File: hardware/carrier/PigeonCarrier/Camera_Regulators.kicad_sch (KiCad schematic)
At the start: 19 parts, among them U4 TPS62933FDRLR

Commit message: carrier progress
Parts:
- removed C31, C32, C39, C40, C41, C42, C44, C45: 10uF, Capacitor_SMD:C_1210_3225Metric, symbol Device:C
- removed C33, C38, C43, C46: 100nF, PCM_JLCPCB:C_0402, symbol PCM_JLCPCB-Capacitors:0402,100nF,(2)
- removed L1: 6.8uH, JLCImport_Auto:CYA1040-6_8UH, symbol JLCImport_Auto:CYA1040-6_8UH
- removed R11, R22: 10kΩ, PCM_JLCPCB:R_0402, symbol PCM_JLCPCB-Resistors:0402,10kΩ
- removed R14: 51kΩ, PCM_JLCPCB:R_0402, symbol PCM_JLCPCB-Resistors:0402,51kΩ
- removed R21: 1.5kΩ, PCM_JLCPCB:R_0402, symbol PCM_JLCPCB-Resistors:0402,1.5kΩ
- removed R23: 0Ω, PCM_JLCPCB:R_0402, symbol PCM_JLCPCB-Resistors:0402,0Ω
- removed U4: TPS62933FDRLR, PigeonVision:SOT-583-8, symbol PigeonVision:TPS62933FDRLR
- added C34, C35: 1uF, PCM_JLCPCB:C_0603, symbol PCM_JLCPCB-Capacitors:0603,1uF
- added C36, C37: 10uF, Capacitor_SMD:C_1210_3225Metric, symbol Device:C
- added R15: 7.5kΩ, PCM_JLCPCB:R_0402, symbol PCM_JLCPCB-Resistors:0402,7.5kΩ
- added R16, R17: 10kΩ, PCM_JLCPCB:R_0402, symbol PCM_JLCPCB-Resistors:0402,10kΩ
- added R18: 22kΩ, PCM_JLCPCB:R_0402, symbol PCM_JLCPCB-Resistors:0402,22kΩ
- added R19: 47kΩ, PCM_JLCPCB:R_0402, symbol PCM_JLCPCB-Resistors:0402,47kΩ
- added R24: 51kΩ, PCM_JLCPCB:R_0402, symbol PCM_JLCPCB-Resistors:0402,51kΩ
- added U6, U7: TLV75801PDRVR, PigeonVision:TI_DRV0006A_WSON-6-1EP_2x2mm_P0.65mm, symbol PigeonVision:TLV75801PDRVR
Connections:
- net GND: now also C34.1, C35.1, C36.2, C37.2, R15.2, R16.1, R17.1, R18.2, U6.3 (GND), U6.7 (GND), U7.3 (GND), U7.7 (GND)
- new net: R15.1, R19.2, U6.2 (FB)
- new net: R18.1, R24.2, U7.2 (FB)
- new net +3V3: C34.2, U7.6 (IN)
- new net 1V8_CAM: C37.1, R24.1, U7.1 (OUT)
- new net 1V8_CAM_EN: R16.2, U7.4 (EN)
- new net 4V_CAM: C36.1, R19.1, U6.1 (OUT)
- new net 4V_CAM_EN: R17.2, U6.4 (EN)
- new net 5V_MAIN: C35.2, U6.6 (IN)
- no-connect marks 1 -> 2
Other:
- note added: "1.825V Output"
- note added: "3.997V Output"
- note added: "3V3 -> 1V8"
- note added: "5V_Main-> 4V"
- note removed: "5.00V Output"
- note removed: "Effective Cap: 56.5uF"
- note removed: "Extra Caps to reduce ripple"
- note removed: "F_sw = 500kHz"
- note removed: "VBAT -> 5V_RF"
- note removed: "t_ss= 14.5ms ~19mA"
- note removed: "~4mV ripple W ESR"

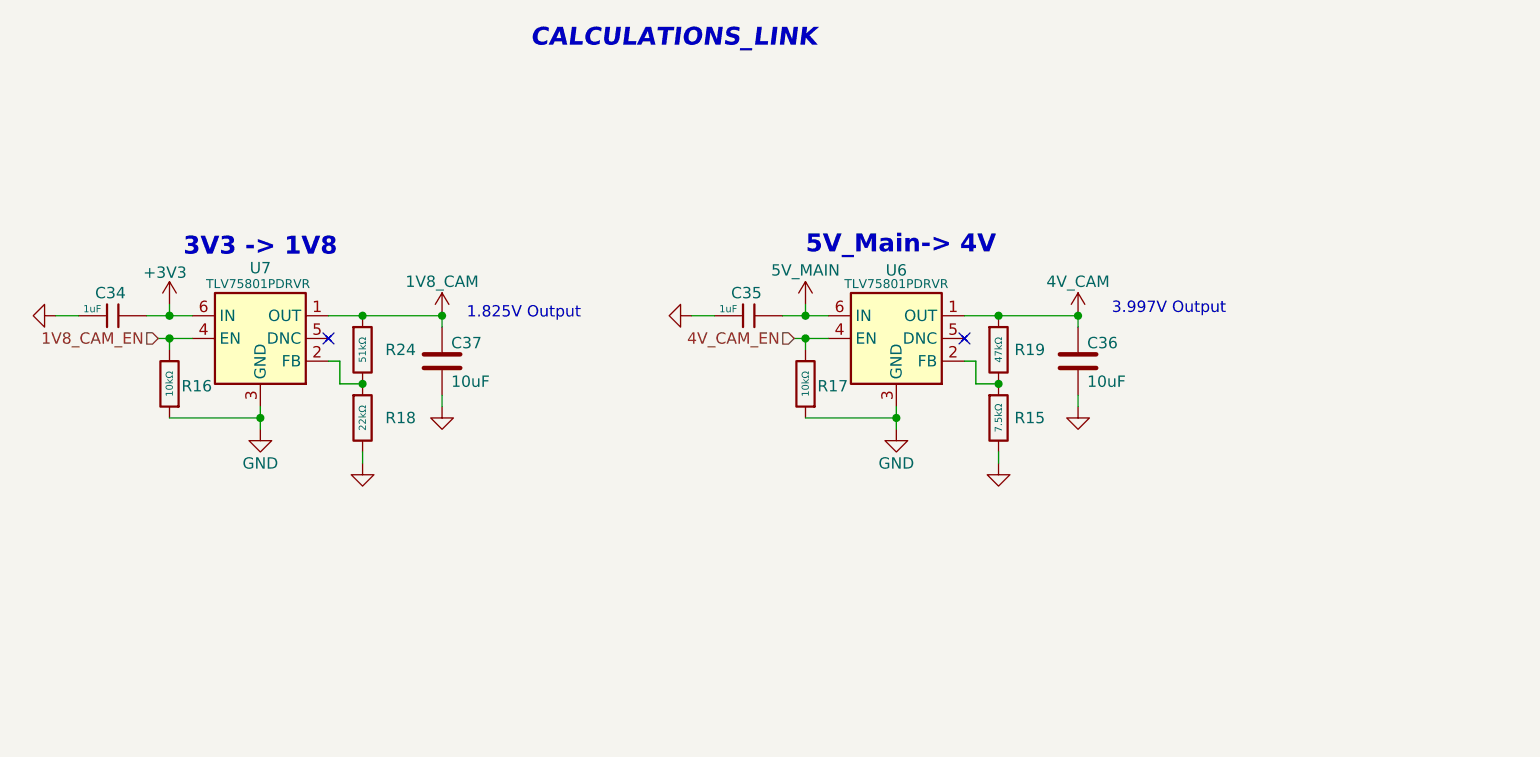
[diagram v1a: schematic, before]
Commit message: Update carrier schematics, parts library, and JLC rules
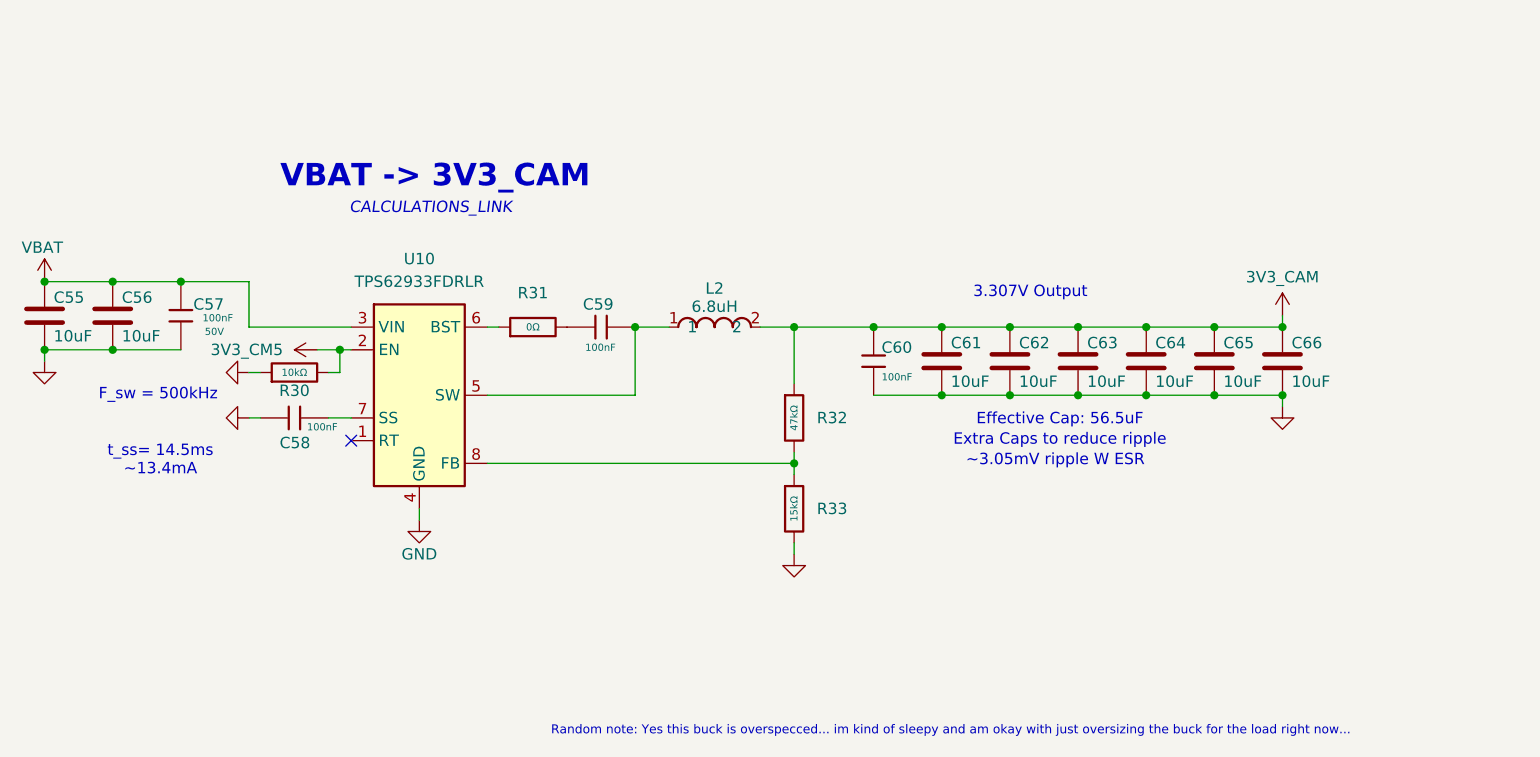
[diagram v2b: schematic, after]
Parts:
- removed C34, C35: 1uF, PCM_JLCPCB:C_0603, symbol PCM_JLCPCB-Capacitors:0603,1uF
- removed C36, C37: 10uF, Capacitor_SMD:C_1210_3225Metric, symbol Device:C
- removed R15: 7.5kΩ, PCM_JLCPCB:R_0402, symbol PCM_JLCPCB-Resistors:0402,7.5kΩ
- removed R16, R17: 10kΩ, PCM_JLCPCB:R_0402, symbol PCM_JLCPCB-Resistors:0402,10kΩ
- removed R18: 22kΩ, PCM_JLCPCB:R_0402, symbol PCM_JLCPCB-Resistors:0402,22kΩ
- removed R19: 47kΩ, PCM_JLCPCB:R_0402, symbol PCM_JLCPCB-Resistors:0402,47kΩ
- removed R24: 51kΩ, PCM_JLCPCB:R_0402, symbol PCM_JLCPCB-Resistors:0402,51kΩ
- removed U6, U7: TLV75801PDRVR, PigeonVision:TI_DRV0006A_WSON-6-1EP_2x2mm_P0.65mm, symbol PigeonVision:TLV75801PDRVR
- added C55, C56, C61, C62, C63, C64, C65, C66: 10uF, Capacitor_SMD:C_1210_3225Metric, symbol Device:C
- added C57, C58, C59, C60: 100nF, PCM_JLCPCB:C_0402, symbol PCM_JLCPCB-Capacitors:0402,100nF,(2)
- added L2: 6.8uH, JLCImport_Auto:CYA1040-6_8UH, symbol JLCImport_Auto:CYA1040-6_8UH
- added R30: 10kΩ, PCM_JLCPCB:R_0402, symbol PCM_JLCPCB-Resistors:0402,10kΩ
- added R31: 0Ω, PCM_JLCPCB:R_0402, symbol PCM_JLCPCB-Resistors:0402,0Ω
- added R32: 47kΩ, PCM_JLCPCB:R_0402, symbol PCM_JLCPCB-Resistors:0402,47kΩ
- added R33: 15kΩ, PCM_JLCPCB:R_0402, symbol PCM_JLCPCB-Resistors:0402,15kΩ
- added U10: TPS62933FDRLR, PigeonVision:SOT-583-8, symbol PigeonVision:TPS62933FDRLR
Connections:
- net GND: now also C55.2, C56.2, C57.1, C58.1, C60.1, C61.2, C62.2, C63.2, C64.2, C65.2, C66.2, R30.1, R33.2, U10.4 (GND)
- new net: C58.2, U10.7 (SS)
- new net: C59.1, L2.1, U10.5 (SW)
- new net: R31.1, U10.6 (BST)
- new net: R32.2, R33.1, U10.8 (FB)
- new net: C59.2, R31.2
- new net 3V3_CAM: C60.2, C61.1, C62.1, C63.1, C64.1, C65.1, C66.1, L2.2, R32.1
- new net 3V3_CM5: R30.2, U10.2 (EN)
- new net VBAT: C55.1, C56.1, C57.2, U10.3 (VIN)
- no-connect marks 2 -> 1
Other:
- note added: "3.307V Output"
- note added: "Effective Cap: 56.5uF"
- note added: "Extra Caps to reduce ripple"
- note added: "F_sw = 500kHz"
- note added: "Random note: Yes this buck is overspecced... im kind of sleepy and am okay with just oversizing the buck for the load right now..."
- note added: "VBAT -> 3V3_CAM"
- note added: "t_ss= 14.5ms ~13.4mA"
- note added: "~3.05mV ripple W ESR"
- note removed: "1.825V Output"
- note removed: "3.997V Output"
- note removed: "3V3 -> 1V8"
- note removed: "5V_Main-> 4V"

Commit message: finished rough layout
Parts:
- C55, C56, C61, C62, C63, C64, C65, C66: MPN (none) -> CL32B106KBJNNNE
- C57, C58, C59, C60: MPN (none) -> CL05B104KB54PNC
- L2: MPN (none) -> CYA1040-6.8UH
- R30: MPN (none) -> 0402WGF1002TCE
- R31: MPN (none) -> 0402WGF0000TCE
- R32: MPN (none) -> 0402WGF4702TCE
- R33: MPN (none) -> 0402WGF1502TCE
